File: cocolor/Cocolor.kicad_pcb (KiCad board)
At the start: 2 copper layers, 30 x 20 mm, 17 parts, among them P1 CONN_01X05, P2 CONN_01X05, U1 TCS3472, U2 LTC4316

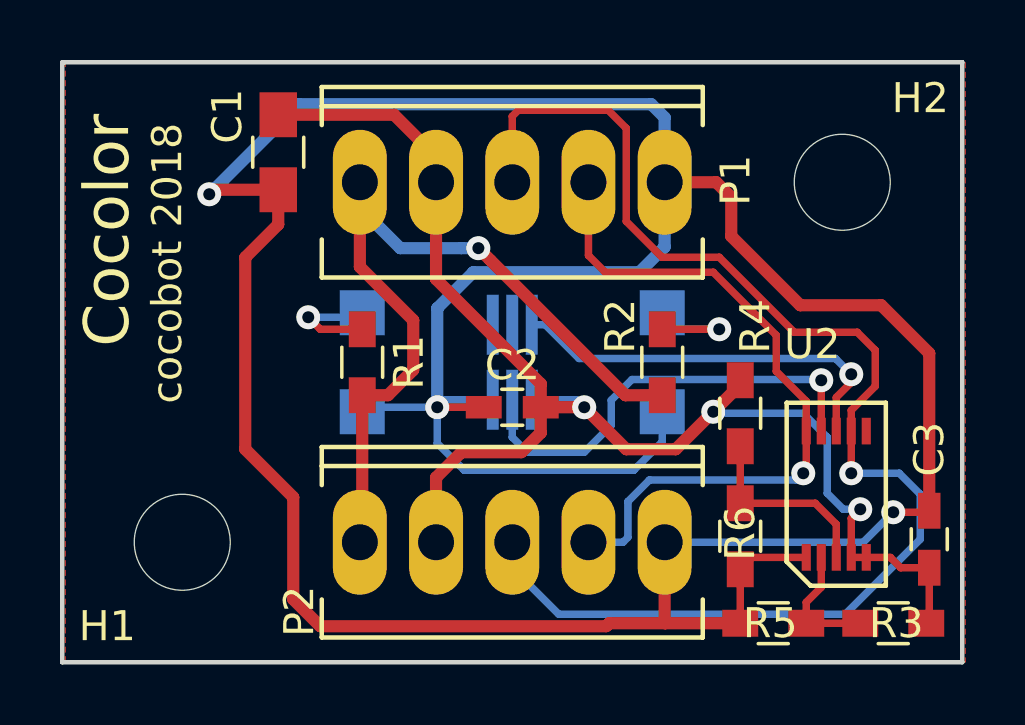
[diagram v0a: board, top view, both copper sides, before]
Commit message: Add 3D file for Cocolor sensor
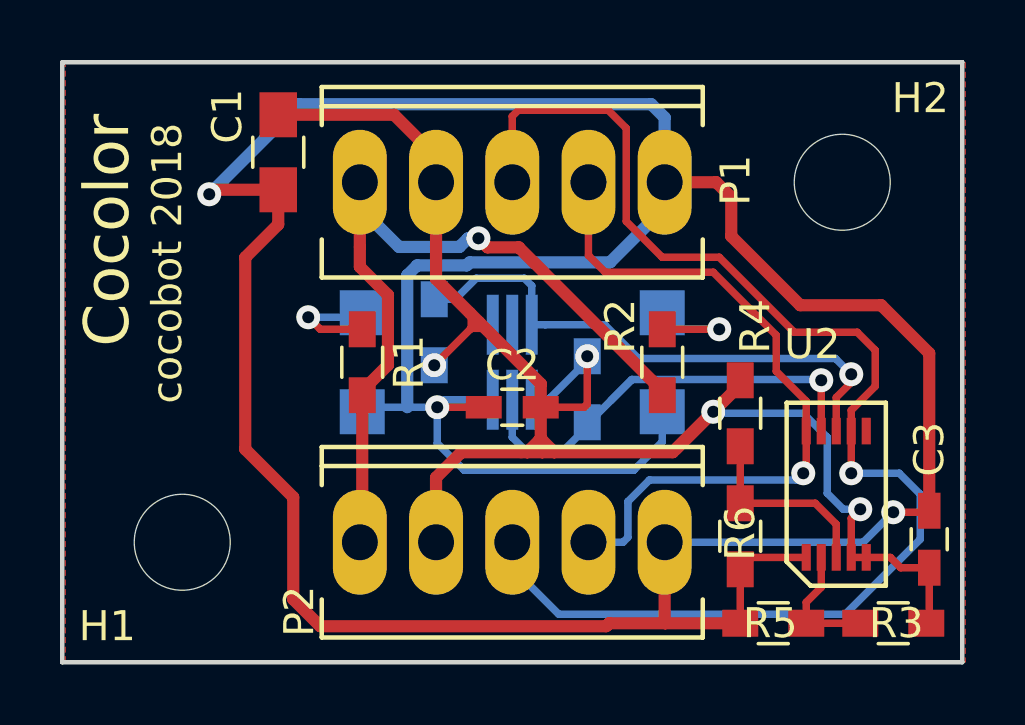
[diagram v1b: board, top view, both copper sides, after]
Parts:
- added R7: R, espitall:R_0603_HandSoldering, B.Cu at (67.5, 60.9)
- added R8: R, espitall:R_0603_HandSoldering, B.Cu at (62.4, 59.0)
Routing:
- net +3V3: track 46.6 -> 56.5 mm, vias 3 -> 4
- net Net-(R8-Pad2): track 13.4 -> 18.4 mm
- net GND: track 115.9 -> 116.8 mm
- net +5V: track 27.5 -> 26.6 mm
- net Net-(R7-Pad2): track 15.0 -> 15.6 mm
